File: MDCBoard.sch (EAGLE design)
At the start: 195 parts, among them J1 JUMPER-SOLDER-CLOSED, J10 USB-C-RECEPTACLE-KOREANHRO, J2 JUMPER-SOLDER-CLOSED, J3 JUMPER-SOLDER-CLOSED, J4 JUMPER-SOLDER-CLOSED, J5 BATTERY-HEADER-MOLEX-781710002, J6 JUMPER-SOLDER-CLOSED, J7 JUMPER-SOLDER-CLOSED, J8 JUMPER-SOLDER-CLOSED, J9 MICROSD-SOCKET, Q1 PMOS-NEXPERIA-SOT1220, Q2 PMOS-NEXPERIA-SOT1220, Q3 PMOS-NEXPERIA-SOT1220, Q4 DIODESINC-DMG2305UX, Q5 DIODESINC-DMG2305UX, Q6 DIODESINC-DMG2305UX, SW1 TACTILE-SWITCH, U1 TI-TPS2116, U10 TI-TPS22919DCK, U11 TI-TPS22919DCK, U12 TI-TPS22919DCK, U13 TI-TPS22919DCK, U14 TI-MSP430FR2433IRGE, U15 NEXPERIA-NXB0102, U16 NEXPERIA-74LVC1G98-MUX-INV-OU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, U17 NEXPERIA-74LVC1G98-MUX-INV-OU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, U18 PANASONIC-EKMB110711X, U19 LATTICE-ICE40HX4K-BG121, U2 DIODESINC-AP7350, U20 WINBOND-W25Q40EW, U21 NEXPERIA-74LVC1G98-OR-INV-INP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, U22 NEXPERIA-74LVC1G98-BUFFER, U23 ON-AR0330CS1C12SPKA0, U24 ALLIANCE-AS4C8M16MSA-6BIN, U25 NEXPERIA-74LVC1G98-INVERTER, U26 STM-STM32F730, U27 DIODESINC-DT1446-04V-7, U3 NEXPERIA-74LVC1G98-NOR, U4 MICROCHIP-MCP7383X, U5 TI-TPS22919DCK, U6 EATON-STN101, U7 TI-TPS62A01, U8 TI-TPS62A01, U9 TI-TPS62A01, X1 EPSON-FC-135, X2 SITIME-SIT8021, X3 SITIME-SIT8021, X4 MDC-CUTOUT, X5 MDC-CUTOUT

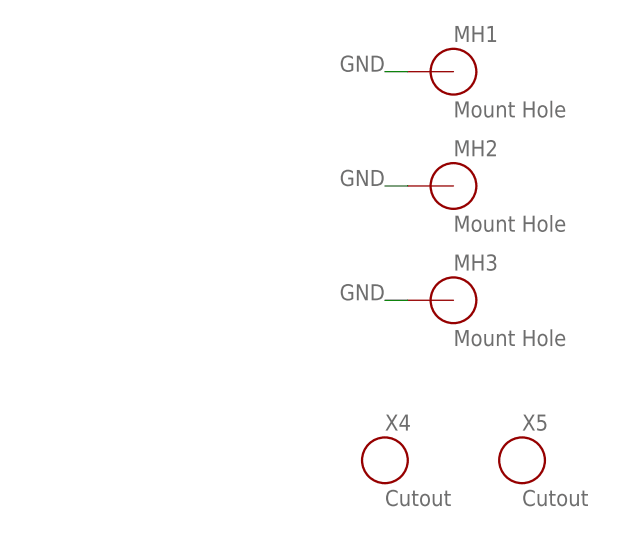
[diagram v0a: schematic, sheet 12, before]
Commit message: Replaced USB-C receptacle with waterproof one. Layout progress.
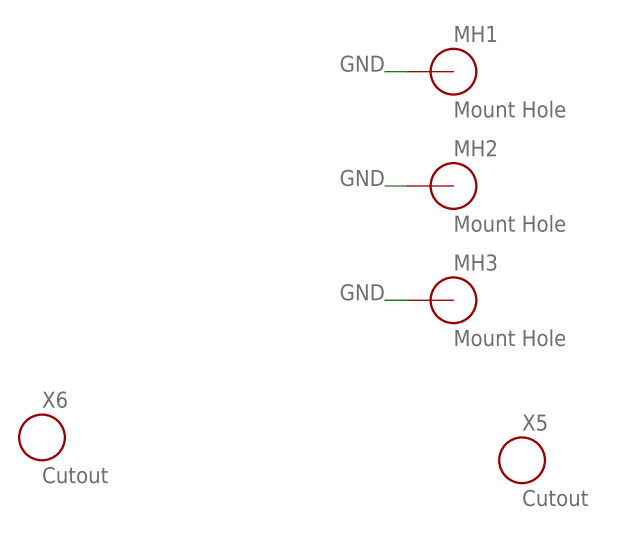
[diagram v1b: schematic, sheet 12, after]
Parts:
- removed J10: USB-C-RECEPTACLE-KOREANHRO, EagleLibrary:USB-C-RECEPTACLE-KOREANHRO
- removed X4: MDC-CUTOUT, EagleLibrary:MDC-CUTOUT
- added J11: USB-C-RECEPTACLE-GSWITCH-7030A, EagleLibrary:USB-C-RECEPTACLE-GSWITCH-7030A
- added X6: MDC-CUTOUT-HALF, EagleLibrary:MDC-CUTOUT-HALF
- X5: value MDC-CUTOUT -> MDC-CUTOUT-FULL; device EagleLibrary:MDC-CUTOUT -> EagleLibrary:MDC-CUTOUT-FULL
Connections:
- net GND: now also J11.GND; no longer J10.GND
- net N$35: now also J11.CC1; no longer J10.CC1
- net N$36: now also J11.CC2; no longer J10.CC2
- net N$54: now also J11.VBUS; no longer J10.VBUS
- net USB_D+: now also J11.D+; no longer J10.D+
- net USB_D-: now also J11.D-; no longer J10.D-
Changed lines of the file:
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@@
 <attribute name="PN" value="STN101050B101"/>
 </part>
-<part name="J10" library="EagleLibrary" deviceset="USB-C-RECEPTACLE" device="-KOREANHRO"/>
 <part name="R42" library="EagleLibrary" deviceset="RESISTOR" device="0402" value="5.1k">
 <attribute name="MFG" value="Yageo"/>
@@
 <part name="U5" library="EagleLibrary" deviceset="TI-TPS22919DCK" device=""/>
 <part name="U15" library="EagleLibrary" deviceset="NEXPERIA-NXB0102" device=""/>
-<part name="X4" library="EagleLibrary" deviceset="MDC-CUTOUT" device=""/>
-<part name="X5" library="EagleLibrary" deviceset="MDC-CUTOUT" device=""/>
+<part name="X5" library="EagleLibrary" deviceset="MDC-CUTOUT" device="-FULL"/>
+<part name="J11" library="EagleLibrary" deviceset="USB-C-RECEPTACLE" device="-GSWITCH-7030A"/>
+<part name="X6" library="EagleLibrary" deviceset="MDC-CUTOUT" device="-HALF"/>
 </parts>
 <sheets>
@@
 <attribute name="NAME" x="45.72" y="-33.02" size="1.778" layer="95" align="top-left"/>
 </instance>
-<instance part="J10" gate="G$1" x="-17.78" y="-5.08" smashed="yes">
-<attribute name="NAME" x="-17.78" y="-4.572" size="1.778" layer="95"/>
-<attribute name="PN" x="-17.78" y="-40.64" size="1.778" layer="95"/>
-</instance>
 <instance part="R42" gate="G$1" x="15.24" y="-27.94" smashed="yes" rot="MR270">
 <attribute name="NAME" x="17.526" y="-26.162" size="1.778" layer="95" rot="MR180"/>
@@
 <attribute name="PN" x="5.08" y="-30.48" size="1.778" layer="96" rot="MR270" display="off"/>
 </instance>
+<instance part="J11" gate="G$1" x="-17.78" y="-5.08" smashed="yes">
+<attribute name="NAME" x="-17.78" y="-4.572" size="1.778" layer="95"/>
+<attribute name="PN" x="-17.78" y="-40.64" size="1.778" layer="95"/>
+</instance>
 </instances>
 <busses>
@@
 <junction x="40.64" y="-10.16"/>
 <pinref part="U27" gate="G$1" pin="GND"/>
-<pinref part="J10" gate="G$1" pin="GND"/>
+<pinref part="J11" gate="G$1" pin="GND"/>
 </segment>
 <segment>
@@
 <wire x1="35.56" y1="-48.26" x2="35.56" y2="-15.24" width="0.1524" layer="91"/>
 <junction x="35.56" y="-15.24"/>
-<pinref part="J10" gate="G$1" pin="D+"/>
+<pinref part="J11" gate="G$1" pin="D+"/>
 </segment>
 </net>
@@
 <wire x1="38.1" y1="-45.72" x2="38.1" y2="-17.78" width="0.1524" layer="91"/>
 <wire x1="38.1" y1="-45.72" x2="43.18" y2="-45.72" width="0.1524" layer="91"/>
-<pinref part="J10" gate="G$1" pin="D-"/>
+<pinref part="J11" gate="G$1" pin="D-"/>
 </segment>
 </net>
@@
 <wire x1="30.48" y1="-53.34" x2="30.48" y2="-7.62" width="0.1524" layer="91"/>
 <junction x="30.48" y="-7.62"/>
-<pinref part="J10" gate="G$1" pin="VBUS"/>
+<pinref part="J11" gate="G$1" pin="VBUS"/>
 </segment>
 </net>
@@
 <net name="N$35" class="0">
 <segment>
-<pinref part="J10" gate="G$1" pin="CC1"/>
 <pinref part="R42" gate="G$1" pin="1"/>
 <wire x1="0" y1="-22.86" x2="15.24" y2="-22.86" width="0.1524" layer="91"/>
+<pinref part="J11" gate="G$1" pin="CC1"/>
 </segment>
 </net>
@@
 <segment>
 <pinref part="R43" gate="G$1" pin="1"/>
-<pinref part="J10" gate="G$1" pin="CC2"/>
 <wire x1="5.08" y1="-25.4" x2="0" y2="-25.4" width="0.1524" layer="91"/>
+<pinref part="J11" gate="G$1" pin="CC2"/>
 </segment>
 </net>
@@
 <attribute name="NAME" x="5.08" y="-22.098" size="1.778" layer="95"/>
 </instance>
-<instance part="X4" gate="G$1" x="-2.54" y="-43.18" smashed="yes">
-<attribute name="NAME" x="-2.54" y="-39.878" size="1.778" layer="95"/>
-</instance>
 <instance part="X5" gate="G$1" x="12.7" y="-43.18" smashed="yes">
 <attribute name="NAME" x="12.7" y="-39.878" size="1.778" layer="95"/>
 </instance>
+<instance part="X6" gate="G$1" x="-40.64" y="-40.64" smashed="yes">
+<attribute name="NAME" x="-40.64" y="-37.338" size="1.778" layer="95"/>
+</instance>
 </instances>

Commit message: Replace left board cutout with 2x cutout-half
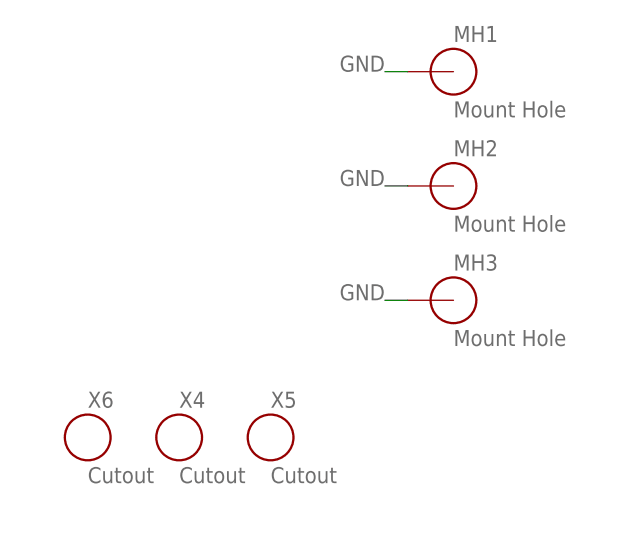
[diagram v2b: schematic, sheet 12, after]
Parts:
- added X4: MDC-CUTOUT-HALF, EagleLibrary:MDC-CUTOUT-HALF
- X5: value MDC-CUTOUT-FULL -> MDC-CUTOUT-HALF; device EagleLibrary:MDC-CUTOUT-FULL -> EagleLibrary:MDC-CUTOUT-HALF
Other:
- moved on the sheet: X5, X6
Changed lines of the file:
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@@
 <part name="U5" library="EagleLibrary" deviceset="TI-TPS22919DCK" device=""/>
 <part name="U15" library="EagleLibrary" deviceset="NEXPERIA-NXB0102" device=""/>
-<part name="X5" library="EagleLibrary" deviceset="MDC-CUTOUT" device="-FULL"/>
 <part name="J11" library="EagleLibrary" deviceset="USB-C-RECEPTACLE" device="-GSWITCH-7030A"/>
 <part name="X6" library="EagleLibrary" deviceset="MDC-CUTOUT" device="-HALF"/>
+<part name="X4" library="EagleLibrary" deviceset="MDC-CUTOUT" device="-HALF"/>
+<part name="X5" library="EagleLibrary" deviceset="MDC-CUTOUT" device="-HALF"/>
 </parts>
 <sheets>
@@
 <attribute name="NAME" x="5.08" y="-22.098" size="1.778" layer="95"/>
 </instance>
-<instance part="X5" gate="G$1" x="12.7" y="-43.18" smashed="yes">
-<attribute name="NAME" x="12.7" y="-39.878" size="1.778" layer="95"/>
+<instance part="X6" gate="G$1" x="-35.56" y="-40.64" smashed="yes">
+<attribute name="NAME" x="-35.56" y="-37.338" size="1.778" layer="95"/>
 </instance>
-<instance part="X6" gate="G$1" x="-40.64" y="-40.64" smashed="yes">
-<attribute name="NAME" x="-40.64" y="-37.338" size="1.778" layer="95"/>
+<instance part="X4" gate="G$1" x="-25.4" y="-40.64" smashed="yes">
+<attribute name="NAME" x="-25.4" y="-37.338" size="1.778" layer="95"/>
+</instance>
+<instance part="X5" gate="G$1" x="-15.24" y="-40.64" smashed="yes">
+<attribute name="NAME" x="-15.24" y="-37.338" size="1.778" layer="95"/>
 </instance>
 </instances>

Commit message: Progress
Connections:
- net GND: now also H1.3; no longer H1.5
- net STM_SWCLK: now also H1.6; no longer H1.4
- net STM_SWDIO: now also H1.5; no longer H1.6
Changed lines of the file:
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@@
-</segment>
-<segment>
-<pinref part="H1" gate="A" pin="5"/>
-<wire x1="233.68" y1="-96.52" x2="236.22" y2="-96.52" width="0.1524" layer="91"/>
-<label x="236.22" y="-96.52" size="1.778" layer="95"/>
 </segment>
 <segment>
@@
 <label x="55.88" y="-271.78" size="1.778" layer="95" align="top-left"/>
 <pinref part="C84" gate="G$1" pin="2"/>
+</segment>
+<segment>
+<wire x1="233.68" y1="-88.9" x2="236.22" y2="-88.9" width="0.1524" layer="91"/>
+<label x="236.22" y="-88.9" size="1.778" layer="95"/>
+<pinref part="H1" gate="A" pin="3"/>
 </segment>
 </net>
@@
 </segment>
 <segment>
-<pinref part="H1" gate="A" pin="6"/>
-<wire x1="233.68" y1="-99.06" x2="236.22" y2="-99.06" width="0.1524" layer="91"/>
-<label x="236.22" y="-99.06" size="1.778" layer="95"/>
+<wire x1="233.68" y1="-96.52" x2="236.22" y2="-96.52" width="0.1524" layer="91"/>
+<label x="236.22" y="-96.52" size="1.778" layer="95"/>
+<pinref part="H1" gate="A" pin="5"/>
 </segment>
 </net>
@@
 </segment>
 <segment>
-<pinref part="H1" gate="A" pin="4"/>
-<wire x1="233.68" y1="-93.98" x2="236.22" y2="-93.98" width="0.1524" layer="91"/>
-<label x="236.22" y="-93.98" size="1.778" layer="95"/>
-</segment>
-</net>
+<wire x1="233.68" y1="-99.06" x2="236.22" y2="-99.06" width="0.1524" layer="91"/>
+<label x="236.22" y="-99.06" size="1.778" layer="95"/>
+<pinref part="H1" gate="A" pin="6"/>
+</segment>
+</net>

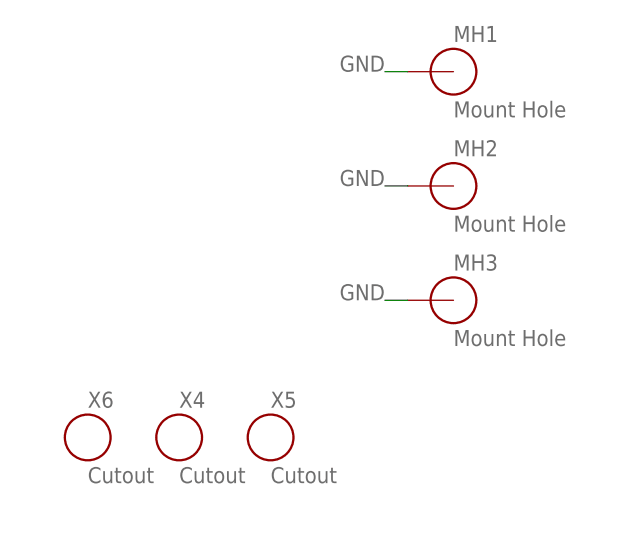
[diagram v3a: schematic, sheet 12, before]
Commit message: Adjust part labels
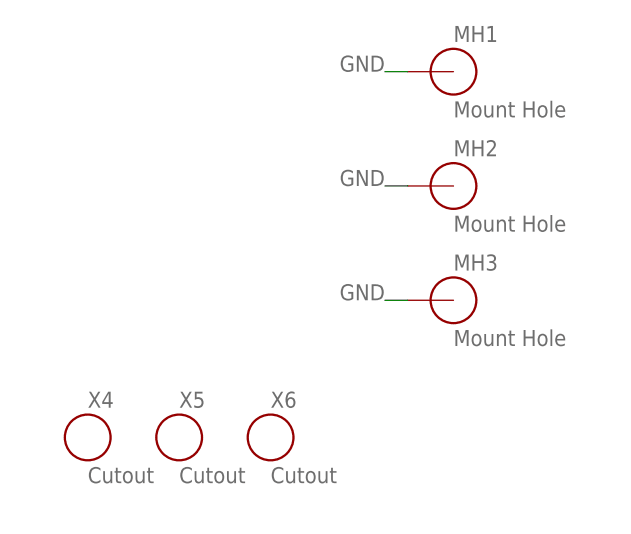
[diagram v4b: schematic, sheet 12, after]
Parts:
- renumbered J11 to J10
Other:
- moved on the sheet: X4, X5, X6
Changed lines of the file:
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@@
 <part name="U5" library="EagleLibrary" deviceset="TI-TPS22919DCK" device=""/>
 <part name="U15" library="EagleLibrary" deviceset="NEXPERIA-NXB0102" device=""/>
-<part name="J11" library="EagleLibrary" deviceset="USB-C-RECEPTACLE" device="-GSWITCH-7030A"/>
-<part name="X6" library="EagleLibrary" deviceset="MDC-CUTOUT" device="-HALF"/>
+<part name="J10" library="EagleLibrary" deviceset="USB-C-RECEPTACLE" device="-GSWITCH-7030A"/>
 <part name="X4" library="EagleLibrary" deviceset="MDC-CUTOUT" device="-HALF"/>
 <part name="X5" library="EagleLibrary" deviceset="MDC-CUTOUT" device="-HALF"/>
+<part name="X6" library="EagleLibrary" deviceset="MDC-CUTOUT" device="-HALF"/>
 </parts>
 <sheets>
@@
 <attribute name="PN" x="5.08" y="-30.48" size="1.778" layer="96" rot="MR270" display="off"/>
 </instance>
-<instance part="J11" gate="G$1" x="-17.78" y="-5.08" smashed="yes">
+<instance part="J10" gate="G$1" x="-17.78" y="-5.08" smashed="yes">
 <attribute name="NAME" x="-17.78" y="-4.572" size="1.778" layer="95"/>
 <attribute name="PN" x="-17.78" y="-40.64" size="1.778" layer="95"/>
@@
 <junction x="40.64" y="-10.16"/>
 <pinref part="U27" gate="G$1" pin="GND"/>
-<pinref part="J11" gate="G$1" pin="GND"/>
+<pinref part="J10" gate="G$1" pin="GND"/>
 </segment>
 <segment>
@@
 <wire x1="35.56" y1="-48.26" x2="35.56" y2="-15.24" width="0.1524" layer="91"/>
 <junction x="35.56" y="-15.24"/>
-<pinref part="J11" gate="G$1" pin="D+"/>
+<pinref part="J10" gate="G$1" pin="D+"/>
 </segment>
 </net>
@@
 <wire x1="38.1" y1="-45.72" x2="38.1" y2="-17.78" width="0.1524" layer="91"/>
 <wire x1="38.1" y1="-45.72" x2="43.18" y2="-45.72" width="0.1524" layer="91"/>
-<pinref part="J11" gate="G$1" pin="D-"/>
+<pinref part="J10" gate="G$1" pin="D-"/>
 </segment>
 </net>
@@
 <wire x1="30.48" y1="-53.34" x2="30.48" y2="-7.62" width="0.1524" layer="91"/>
 <junction x="30.48" y="-7.62"/>
-<pinref part="J11" gate="G$1" pin="VBUS"/>
+<pinref part="J10" gate="G$1" pin="VBUS"/>
 </segment>
 </net>
@@
 <pinref part="R42" gate="G$1" pin="1"/>
 <wire x1="0" y1="-22.86" x2="15.24" y2="-22.86" width="0.1524" layer="91"/>
-<pinref part="J11" gate="G$1" pin="CC1"/>
+<pinref part="J10" gate="G$1" pin="CC1"/>
 </segment>
 </net>
@@
 <pinref part="R43" gate="G$1" pin="1"/>
 <wire x1="5.08" y1="-25.4" x2="0" y2="-25.4" width="0.1524" layer="91"/>
-<pinref part="J11" gate="G$1" pin="CC2"/>
+<pinref part="J10" gate="G$1" pin="CC2"/>
 </segment>
 </net>
@@
 <attribute name="NAME" x="5.08" y="-22.098" size="1.778" layer="95"/>
 </instance>
-<instance part="X6" gate="G$1" x="-35.56" y="-40.64" smashed="yes">
+<instance part="X4" gate="G$1" x="-35.56" y="-40.64" smashed="yes">
 <attribute name="NAME" x="-35.56" y="-37.338" size="1.778" layer="95"/>
 </instance>
-<instance part="X4" gate="G$1" x="-25.4" y="-40.64" smashed="yes">
+<instance part="X5" gate="G$1" x="-25.4" y="-40.64" smashed="yes">
 <attribute name="NAME" x="-25.4" y="-37.338" size="1.778" layer="95"/>
 </instance>
-<instance part="X5" gate="G$1" x="-15.24" y="-40.64" smashed="yes">
+<instance part="X6" gate="G$1" x="-15.24" y="-40.64" smashed="yes">
 <attribute name="NAME" x="-15.24" y="-37.338" size="1.778" layer="95"/>
 </instance>

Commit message: Add PN2 to Q1/Q2/Q3
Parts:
- Q1, Q2, Q3: PN2 (none) -> PMPB16EP
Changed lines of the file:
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@@
 <part name="Q1" library="EagleLibrary" deviceset="PMOS" device="-NEXPERIA-SOT1220">
 <attribute name="PN" value="PMPB10UPX"/>
+<attribute name="PN2" value="PMPB16EP"/>
 </part>
 <part name="J3" library="EagleLibrary" deviceset="JUMPER" device="-SOLDER-CLOSED" value="JUMPER-SOLDER-CLOSED"/>
@@
 <part name="Q3" library="EagleLibrary" deviceset="PMOS" device="-NEXPERIA-SOT1220">
 <attribute name="PN" value="PMPB10UPX"/>
+<attribute name="PN2" value="PMPB16EP"/>
 </part>
 <part name="Q2" library="EagleLibrary" deviceset="PMOS" device="-NEXPERIA-SOT1220">
 <attribute name="PN" value="PMPB10UPX"/>
+<attribute name="PN2" value="PMPB16EP"/>
 </part>
 <part name="R11" library="EagleLibrary" deviceset="RESISTOR" device="0402" value="100k">
@@
 <attribute name="NAME" x="318.77" y="399.542" size="1.778" layer="95" rot="MR0" align="bottom-right"/>
 <attribute name="PN" x="287.02" y="609.6" size="1.778" layer="96" rot="MR0" display="off"/>
+<attribute name="PN2" x="320.04" y="396.24" size="1.778" layer="96" rot="MR0" display="off"/>
 </instance>
 <instance part="J3" gate="G$1" x="360.68" y="401.32" smashed="yes">
@@
 <attribute name="NAME" x="219.964" y="364.744" size="1.778" layer="95" align="bottom-right"/>
 <attribute name="PN" x="220.98" y="355.6" size="1.778" layer="96" rot="R90" display="off"/>
+<attribute name="PN2" x="220.98" y="355.6" size="1.778" layer="96" rot="R90" display="off"/>
 </instance>
 <instance part="Q2" gate="G$1" x="195.58" y="355.6" smashed="yes" rot="MR90">
 <attribute name="NAME" x="196.596" y="364.744" size="1.778" layer="95" rot="MR0" align="bottom-right"/>
 <attribute name="PN" x="195.58" y="355.6" size="1.778" layer="96" rot="MR90" display="off"/>
+<attribute name="PN2" x="195.58" y="355.6" size="1.778" layer="96" rot="MR90" display="off"/>
 </instance>
 <instance part="R11" gate="G$1" x="220.98" y="345.44" smashed="yes" rot="MR270">

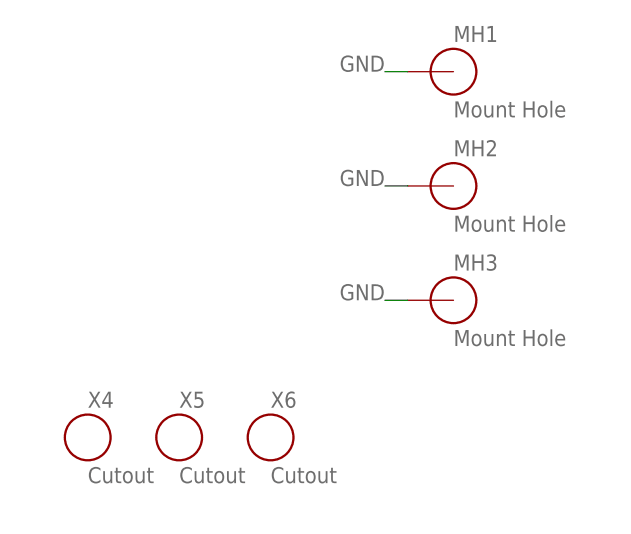
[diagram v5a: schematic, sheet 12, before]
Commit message: Update MDC-CUTOUT prefix: X -> MH
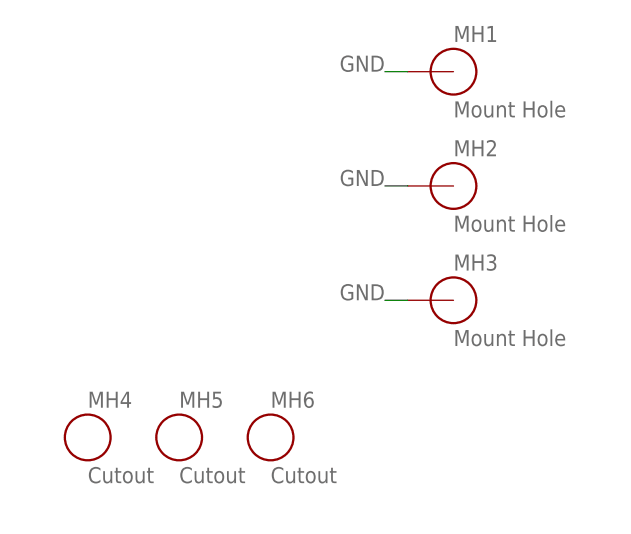
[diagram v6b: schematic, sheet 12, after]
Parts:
- renumbered X4 to MH4, X5 to MH5, X6 to MH6
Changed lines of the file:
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@@
 <part name="U15" library="EagleLibrary" deviceset="NEXPERIA-NXB0102" device=""/>
 <part name="J10" library="EagleLibrary" deviceset="USB-C-RECEPTACLE" device="-GSWITCH-7030A"/>
-<part name="X4" library="EagleLibrary" deviceset="MDC-CUTOUT" device="-HALF"/>
-<part name="X5" library="EagleLibrary" deviceset="MDC-CUTOUT" device="-HALF"/>
-<part name="X6" library="EagleLibrary" deviceset="MDC-CUTOUT" device="-HALF"/>
+<part name="MH4" library="EagleLibrary" deviceset="MDC-CUTOUT" device="-HALF"/>
+<part name="MH5" library="EagleLibrary" deviceset="MDC-CUTOUT" device="-HALF"/>
+<part name="MH6" library="EagleLibrary" deviceset="MDC-CUTOUT" device="-HALF"/>
 </parts>
 <sheets>
@@
 <attribute name="NAME" x="5.08" y="-22.098" size="1.778" layer="95"/>
 </instance>
-<instance part="X4" gate="G$1" x="-35.56" y="-40.64" smashed="yes">
+<instance part="MH4" gate="G$1" x="-35.56" y="-40.64" smashed="yes">
 <attribute name="NAME" x="-35.56" y="-37.338" size="1.778" layer="95"/>
 </instance>
-<instance part="X5" gate="G$1" x="-25.4" y="-40.64" smashed="yes">
+<instance part="MH5" gate="G$1" x="-25.4" y="-40.64" smashed="yes">
 <attribute name="NAME" x="-25.4" y="-37.338" size="1.778" layer="95"/>
 </instance>
-<instance part="X6" gate="G$1" x="-15.24" y="-40.64" smashed="yes">
+<instance part="MH6" gate="G$1" x="-15.24" y="-40.64" smashed="yes">
 <attribute name="NAME" x="-15.24" y="-37.338" size="1.778" layer="95"/>
 </instance>

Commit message: Add assembly attributes to schematic+board devices. Needs some corrections.
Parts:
- C1, C10, C11, C12, C13, C14, C15, C16, C17, C18, C19, C2, C20, C21, C22, C23, C24, C25, C26, C27, C28, C29, C3, C30, C31, C32, C33, C34, C35, C36, C37, C38, C39, C4, C40, C41, C42, C43, C44, C45, C46, C47, C48, C49, C5, C50, C51, C52, C53, C54, C55, C56, C57, C58, C59, C6, C60, C61, C62, C63, C64, C65, C66, C67, C68, C69, C7, C70, C71, C72, C73, C74, C75, C76, C77, C78, C79, C8, C80, C81, C82, C83, C84, C85, C86, C87, C9, D1, FB1, H1, J1, J10, J2, J3, J4, J5, J6, J7, J8, J9, L1, L2, L3, LED1, LED2, LED3, LED4, LED5, LED6, MH1, MH2, MH3, MH4, MH5, MH6, Q1, Q2, Q3, Q4, Q5, Q6, R1, R10, R11, R12, R13, R14, R15, R16, R17, R18, R19, R2, R20, R21, R22, R23, R24, R25, R26, R27, R28, R29, R3, R30, R31, R32, R33, R34, R35, R36, R37, R38, R39, R4, R40, R41, R42, R43, R5, R6, R7, R8, R9, SW1, TP1, U1, U10, U11, U12, U13, U14, U15, U16, U17, U18, U19, U2, U20, U21, U22, U23, U24, U25, U26, U27, U3, U4, U5, U6, U7, U8, U9, X1, X2, X3: AS-MOUNT (none) -> 1; AS-MOUNT-NEXTPCB (none) -> 1; AS-OUR-STOCK (none) -> 0

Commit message: Correct assembly attributes
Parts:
- D1, FB1, Q1, Q2, Q3, Q4, Q5, Q6, SW1, U10, U11, U12, U13, U16, U17, U2, U21, U22, U25, U27, U3, U5, U6, U7, U8, U9: AS-OUR-STOCK 0 -> 1
- H1, J1, J2, J3, J4, J6, J7, J8, LED3, LED4, LED5, LED6, MH1, MH2, MH3, MH4, MH5, MH6, TP1: AS-MOUNT 1 -> 0; AS-MOUNT-NEXTPCB 1 -> 0
- J10, U1, U14, U18, U19, U20, U23, U24, U26, U4, X1, X2, X3: AS-MOUNT-NEXTPCB 1 -> 0
